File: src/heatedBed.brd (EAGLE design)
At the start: 100 x 100 mm, 18 parts

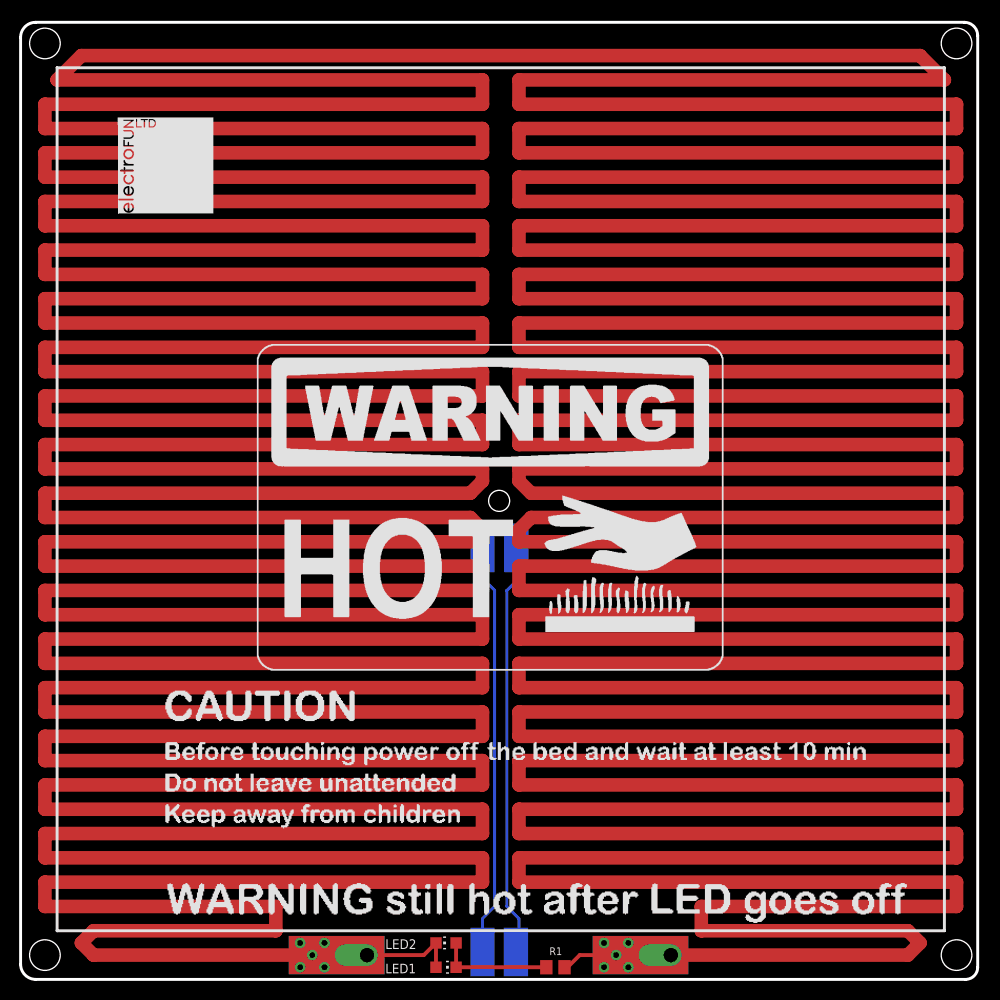
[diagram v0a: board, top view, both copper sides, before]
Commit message: Updated PCB for bottom mount LEDs
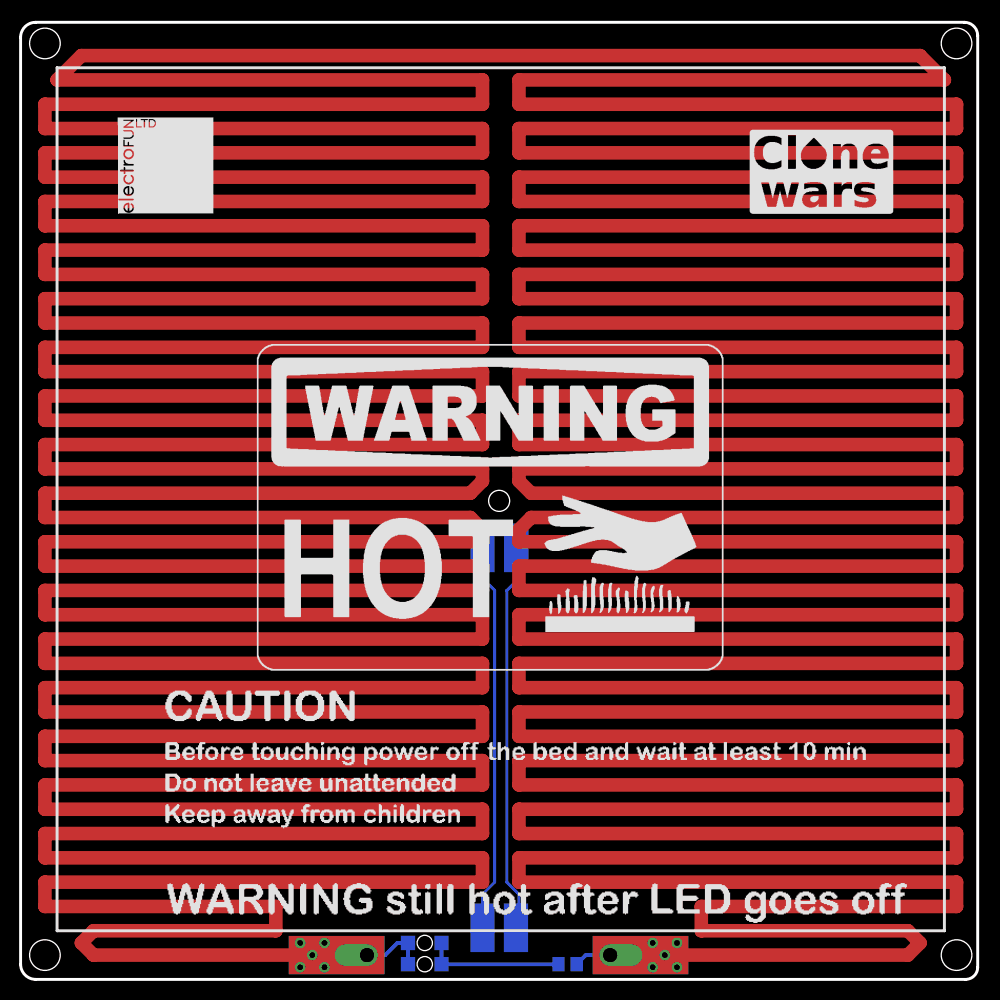
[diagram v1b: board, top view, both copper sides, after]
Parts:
- removed LED1, LED2: (no value), led:CHIP-LED0805
- added L1: 597-6001-607F, led:CHIPLED_1206_REVERSE
- added L2: (no value), led:CHIPLED_1206_REVERSE
- added P2: LONG_PAD, fmc:LONG_PAD
- U$3: value LONG_PAD -> (none); device fmc:LONG_PAD -> fmc:CLONE_WARS
- moved U$3 78.3 mm to (76.2, 80.0)
- moved PAD3 2.54 mm to (48.3, 5.40)
- moved PAD4 2.54 mm to (51.8, 5.40)
- moved R1 1.31 mm to (57.1, 1.59), flipped to the bottom, turned to 180 degrees
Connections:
- removed net N$1: LED1.C, LED2.A, R1.2, U$2.P$1, U$2.P$2, U$2.P$3, U$3.P$1, U$3.P$2, U$3.P$3
- new net P1: L1.C, L2.A, P2.P$1, P2.P$2, P2.P$3, R1.2, U$2.P$1, U$2.P$2, U$2.P$3
- net N$4: now also L1.A, L2.C; no longer LED1.A, LED2.C
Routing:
- net N$1: track 3549.7 -> 0.00 mm, vias 10 -> 0
- net P1: track 0.00 -> 3548.4 mm, vias 0 -> 10
- net N$5: track 43.3 -> 40.7 mm
- net N$3: track 44.5 -> 42.0 mm
- net N$4: track 12.0 -> 14.4 mm

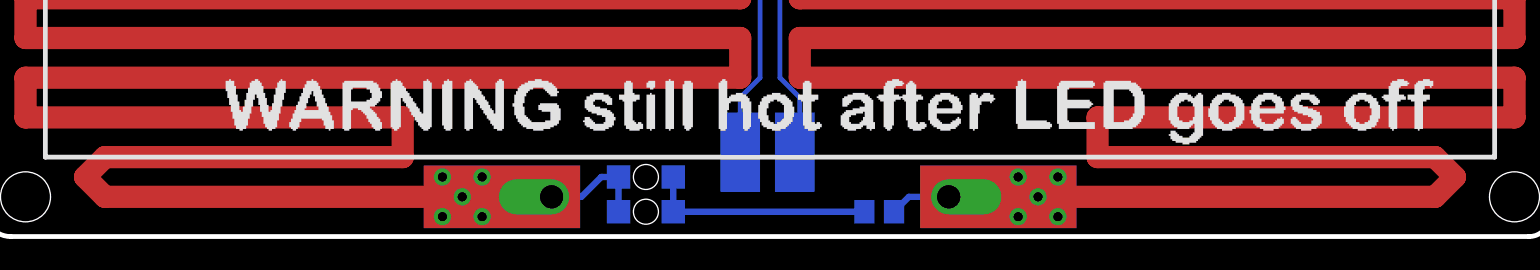
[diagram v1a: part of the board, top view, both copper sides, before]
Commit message: Updated silk screen for production prototype run.
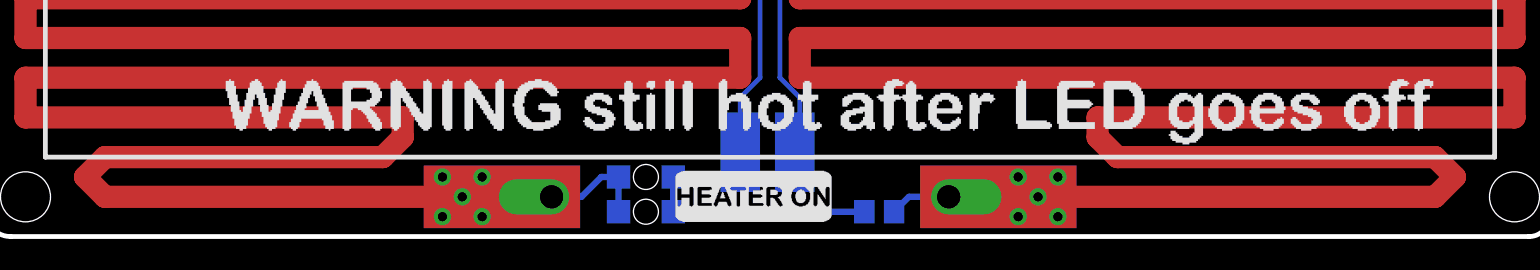
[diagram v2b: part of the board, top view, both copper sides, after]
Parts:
- added U$9: (no value), fmc:HEATERON
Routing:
- net P1: track 3548.4 -> 3547.0 mm
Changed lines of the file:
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@@
 <elements>
 <element name="L1" library="led" package="CHIPLED_1206_REVERSE" value="597-6001-607F" x="42.2275" y="3.81" smashed="yes" rot="MR270">
-<attribute name="NAME" x="36.5125" y="4.445" size="1" layer="26" ratio="12" rot="MR180"/>
+<attribute name="NAME" x="37.7825" y="4.445" size="1" layer="26" ratio="12" rot="MR180"/>
 <attribute name="VALUE" x="43.4975" y="1.27" size="1.27" layer="28" rot="MR0"/>
 </element>
 <element name="L2" library="led" package="CHIPLED_1206_REVERSE" value="" x="42.2275" y="1.5875" smashed="yes" rot="MR90">
-<attribute name="NAME" x="36.5125" y="2.2225" size="1.016" layer="26" ratio="12" rot="MR180"/>
+<attribute name="NAME" x="37.7825" y="2.2225" size="1.016" layer="26" ratio="12" rot="MR180"/>
 <attribute name="VALUE" x="40.9575" y="4.1275" size="1.27" layer="28" rot="MR180"/>
 </element>
 <element name="R1" library="rcl" package="R0805" value="2K2" x="57.15" y="1.5875" smashed="yes" rot="MR180">
-<attribute name="NAME" x="56.8325" y="3.4925" size="0.8128" layer="26" ratio="12" rot="MR180"/>
+<attribute name="NAME" x="56.1975" y="3.4925" size="0.8128" layer="26" ratio="12" rot="MR180"/>
 <attribute name="VALUE" x="56.515" y="4.1275" size="1.27" layer="28" rot="MR180"/>
 </element>
@@
 <element name="U$8" library="fmc" package="BOARD_REF" value="" x="36.195" y="68.2625" rot="MR0"/>
 <element name="U$3" library="fmc" package="CLONE_WARS" value="" x="76.2" y="80.01"/>
+<element name="U$9" library="fmc" package="HEATERON" value="" x="44.1325" y="0.9525"/>
 </elements>
 <signals>
@@
 <wire x1="92.71" y1="2.54" x2="93.98" y2="3.81" width="1.4224" layer="1"/>
 <wire x1="93.98" y1="3.81" x2="92.71" y2="5.08" width="1.4224" layer="1"/>
-<wire x1="92.71" y1="5.08" x2="71.12" y2="5.08" width="1.4224" layer="1"/>
-<wire x1="71.12" y1="5.08" x2="71.12" y2="7.62" width="1.4224" layer="1"/>
 <wire x1="71.12" y1="7.62" x2="97.79" y2="7.62" width="1.4224" layer="1"/>
 <wire x1="97.79" y1="7.62" x2="97.79" y2="10.16" width="1.4224" layer="1"/>
@@
 <wire x1="2.54" y1="10.16" x2="2.54" y2="7.62" width="1.4224" layer="1"/>
 <wire x1="2.54" y1="7.62" x2="26.67" y2="7.62" width="1.4224" layer="1"/>
-<wire x1="26.67" y1="5.08" x2="7.62" y2="5.08" width="1.4224" layer="1"/>
 <wire x1="7.62" y1="5.08" x2="6.35" y2="3.81" width="1.4224" layer="1"/>
 <wire x1="6.35" y1="3.81" x2="7.62" y2="2.54" width="1.4224" layer="1"/>
 <wire x1="7.62" y1="2.54" x2="33.02" y2="2.54" width="1.4224" layer="1"/>
-<wire x1="26.67" y1="7.62" x2="26.67" y2="5.08" width="1.4224" layer="1"/>
 <contactref element="U$2" pad="P$2"/>
 <contactref element="U$2" pad="P$3"/>
@@
 <wire x1="53.34" y1="48.26" x2="52.07" y2="46.99" width="1.4224" layer="1"/>
 <wire x1="52.07" y1="46.99" x2="52.07" y2="45.72" width="1.4224" layer="1"/>
+<wire x1="61.595" y1="2.54" x2="59.0525" y2="2.54" width="0.4064" layer="16"/>
+<wire x1="59.0525" y1="2.54" x2="58.1" y2="1.5875" width="0.4064" layer="16"/>
+<wire x1="40.4775" y1="3.81" x2="40.64" y2="3.81" width="0.4064" layer="16"/>
+<wire x1="40.4775" y1="3.81" x2="39.37" y2="3.81" width="0.4064" layer="16"/>
+<wire x1="39.37" y1="3.81" x2="38.1" y2="2.54" width="0.4064" layer="16"/>
+<wire x1="38.1" y1="2.54" x2="36.195" y2="2.54" width="0.4064" layer="16"/>
+<wire x1="40.4775" y1="3.81" x2="40.4775" y2="1.5875" width="0.4064" layer="16"/>
+<wire x1="26.67" y1="7.62" x2="26.67" y2="6.35" width="1.4224" layer="1"/>
+<wire x1="26.67" y1="6.35" x2="25.4" y2="5.08" width="1.4224" layer="1"/>
+<wire x1="25.4" y1="5.08" x2="7.62" y2="5.08" width="1.4224" layer="1"/>
+<wire x1="71.12" y1="7.62" x2="71.12" y2="6.35" width="1.4224" layer="1"/>
+<wire x1="71.12" y1="6.35" x2="72.39" y2="5.08" width="1.4224" layer="1"/>
+<wire x1="72.39" y1="5.08" x2="92.71" y2="5.08" width="1.4224" layer="1"/>
 <wire x1="67.31" y1="2.54" x2="68.58" y2="3.81" width="0" layer="19" extent="1-1"/>
 <wire x1="66.04" y1="3.81" x2="67.31" y2="2.54" width="0" layer="19" extent="1-1"/>
@@
 <wire x1="31.75" y1="1.27" x2="33.02" y2="2.54" width="0" layer="19" extent="1-1"/>
 <wire x1="29.21" y1="1.27" x2="30.48" y2="2.54" width="0" layer="19" extent="1-1"/>
-<wire x1="61.595" y1="2.54" x2="59.0525" y2="2.54" width="0.4064" layer="16"/>
-<wire x1="59.0525" y1="2.54" x2="58.1" y2="1.5875" width="0.4064" layer="16"/>
-<wire x1="40.4775" y1="3.81" x2="40.64" y2="3.81" width="0.4064" layer="16"/>
-<wire x1="40.4775" y1="3.81" x2="39.37" y2="3.81" width="0.4064" layer="16"/>
-<wire x1="39.37" y1="3.81" x2="38.1" y2="2.54" width="0.4064" layer="16"/>
-<wire x1="38.1" y1="2.54" x2="36.195" y2="2.54" width="0.4064" layer="16"/>
-<wire x1="40.4775" y1="3.81" x2="40.4775" y2="1.5875" width="0.4064" layer="16"/>
 </signal>
 <signal name="N$4">
